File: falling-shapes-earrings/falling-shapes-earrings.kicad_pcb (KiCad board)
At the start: 2 copper layers, 25 x 41.5 mm, 33 parts, among them U1 ATTINY85-20SUR

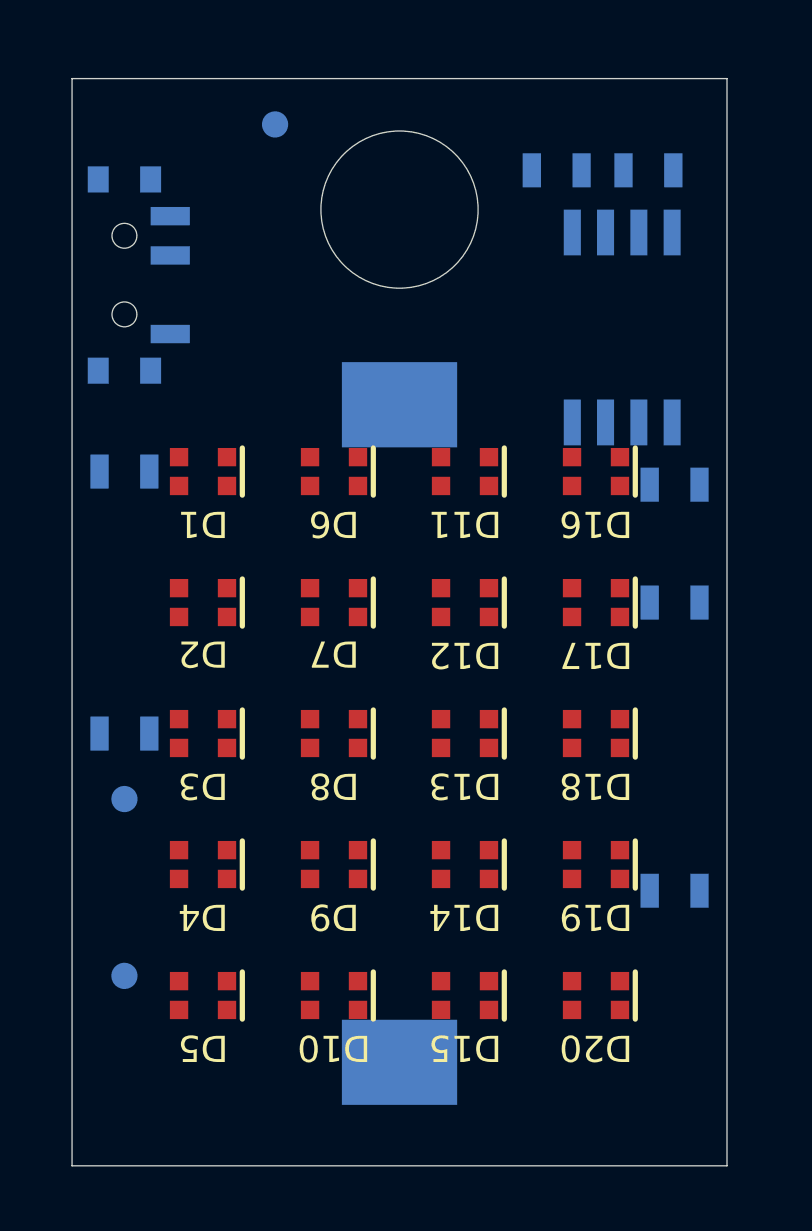
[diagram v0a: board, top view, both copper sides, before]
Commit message: Update falling-shapes-earrings.kicad_pcb
Ran design rule without violation
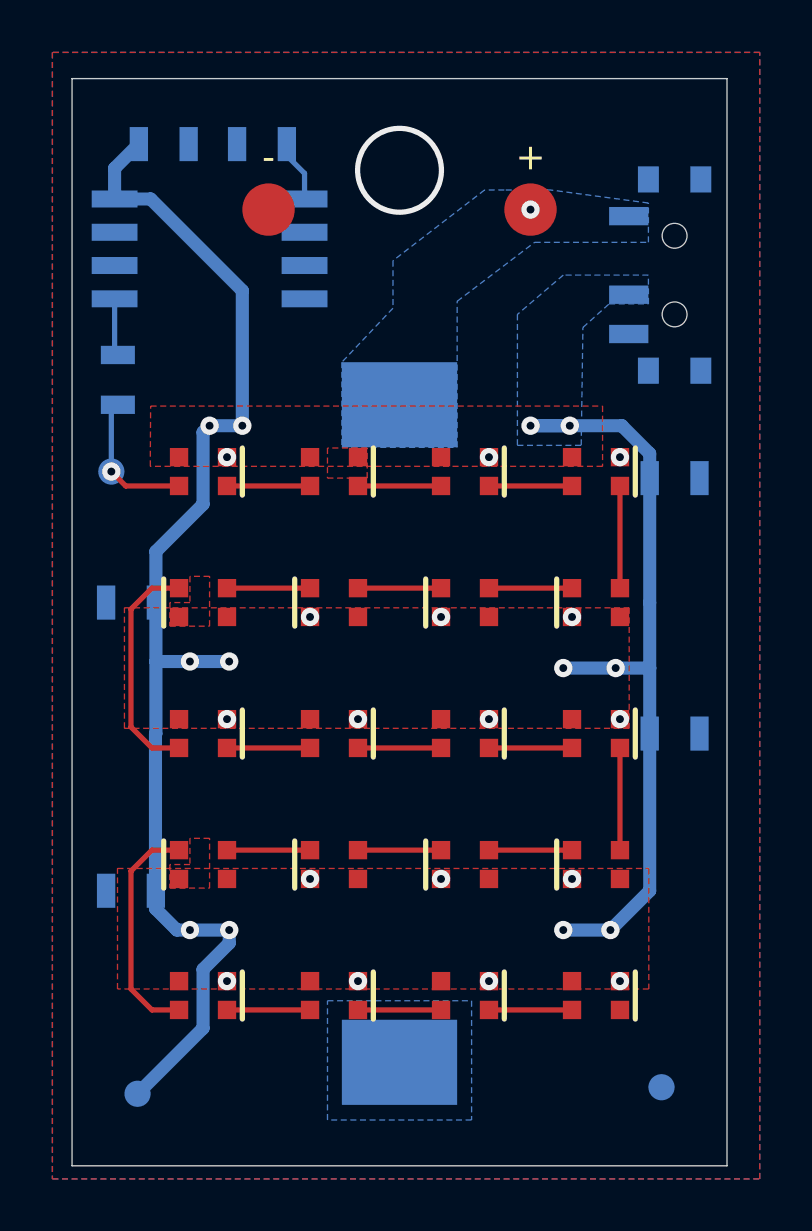
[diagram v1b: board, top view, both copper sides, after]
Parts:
- added TP4: +, Test Points:2mm Test Pad, F.Cu at (82.5, 70.0)
- added TP5: -, Test Points:2mm Test Pad, F.Cu at (72.5, 70.0)
- TP1, TP3: footprint Test Points:Test Pad -> Test Points:1mm Test Pad
- TP2: value ${NET_NAME(1)} -> PWR; footprint Test Points:Test Pad -> Test Points:1mm Test Pad
- moved C2 21.0 mm to (88.0, 80.2), turned to 180 degrees
- moved C4 21.0 mm to (88.0, 90.0)
- moved S1 21.0 mm to (88.0, 72.5), turned to -90 degrees
- moved TP3 20.9 mm to (87.5, 103.5), turned to 180 degrees
- moved C3 20.8 mm to (67.2, 85.0)
- moved C5 20.8 mm to (67.2, 96.0), turned to 0 degrees
- moved R1 20.4 mm to (72.2, 67.5)
- moved R2 18.6 mm to (66.8, 76.5), turned to -90 degrees
- moved C1 18.5 mm to (68.5, 67.5), turned to 180 degrees
- moved U1 16.0 mm to (70.2, 71.5), turned to 180 degrees
- moved D17 15.0 mm to (70.0, 85.0), turned to 0 degrees
- moved D19 15.0 mm to (70.0, 95.0), turned to 0 degrees
- moved D2 15.0 mm to (85.0, 85.0), turned to 0 degrees
- moved D4 15.0 mm to (85.0, 95.0), turned to 0 degrees
- moved TP1 14.7 mm to (66.5, 80.0), turned to 0 degrees
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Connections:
- net Net-(S1-Pad1) renamed /COIN_PWR
- R1 pad 1: 3.3V -> GNDREF
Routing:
- net 3.3V: track 0.00 -> 78.3 mm, vias 0 -> 12
- net Net-(D19-DO): track 0.00 -> 8.83 mm
- net Net-(D17-DO): track 0.00 -> 8.83 mm
- net /LED_DAT: track 0.00 -> 5.47 mm, vias 0 -> 1
- net Net-(D18-DO): track 0.00 -> 3.90 mm
- net Net-(D16-DO): track 0.00 -> 3.90 mm
- net Net-(D4-DO): track 0.00 -> 3.17 mm
- net Net-(D3-DO): track 0.00 -> 3.17 mm
- net Net-(D2-DO): track 0.00 -> 3.17 mm
- net Net-(D15-DO): track 0.00 -> 3.17 mm
- net Net-(D14-DO): track 0.00 -> 3.17 mm
- net Net-(D14-DI): track 0.00 -> 3.17 mm
- net Net-(D13-DO): track 0.00 -> 3.17 mm
- net Net-(D13-DI): track 0.00 -> 3.17 mm
- net Net-(D12-DO): track 0.00 -> 3.17 mm
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- added copper zone on B.Cu, net /COIN_PWR
- added copper zone on B.Cu, net 3.3V
- added copper zone on F.Cu, net 3.3V
- added copper zone on B.Cu, net GNDREF
- added copper zone on F.Cu, net GNDREF
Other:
- outline, holes or cut-outs redrawn

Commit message: Update falling-shapes-earrings.kicad_pcb
Finilised PCB and ran drc (clean)
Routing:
- net GNDREF: vias 17 -> 48
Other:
- board text added: "DES: TSA"
